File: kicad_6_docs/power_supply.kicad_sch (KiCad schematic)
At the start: 56 parts, among them J7 iec_power_entry, T1 power_transformer, U1 RC4558, U10 RC4558, U11 TL072, U12 TL072, U13 TL072, U14 SSI2164, U15 TL072, U16 TL072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

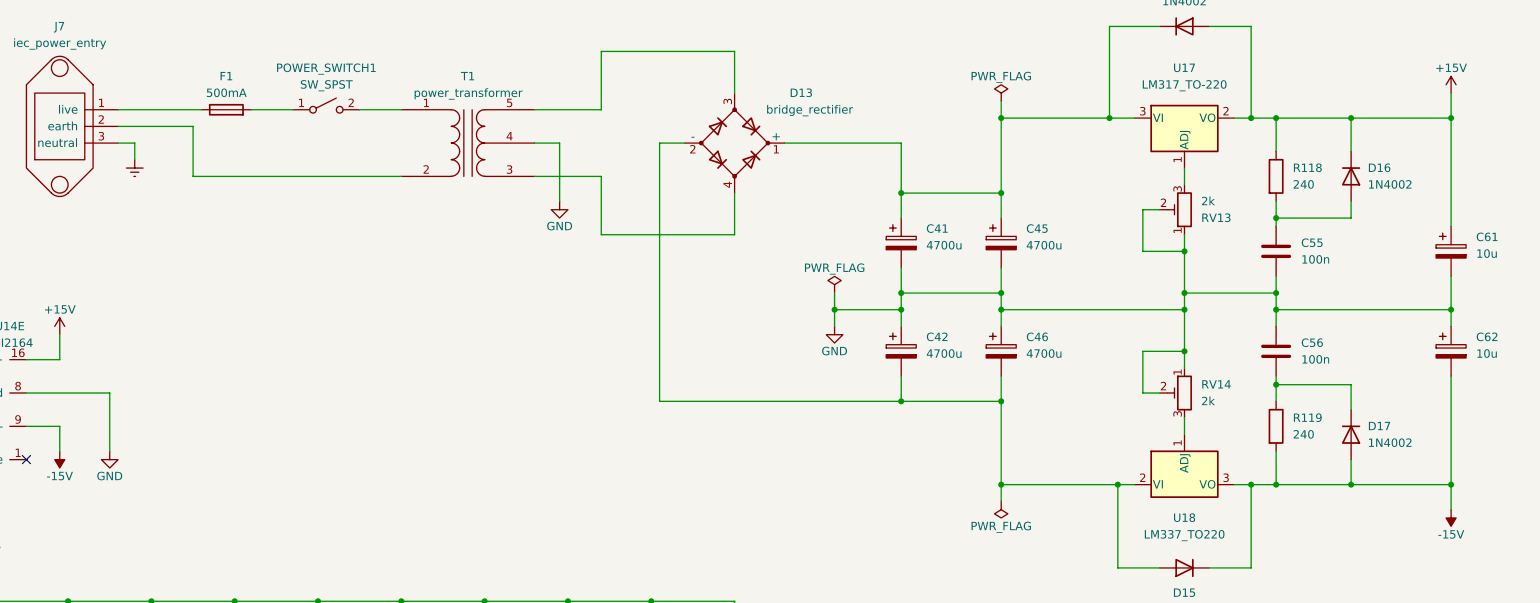
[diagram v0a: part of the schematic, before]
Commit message: Fix power supply errors, tidy up schematic
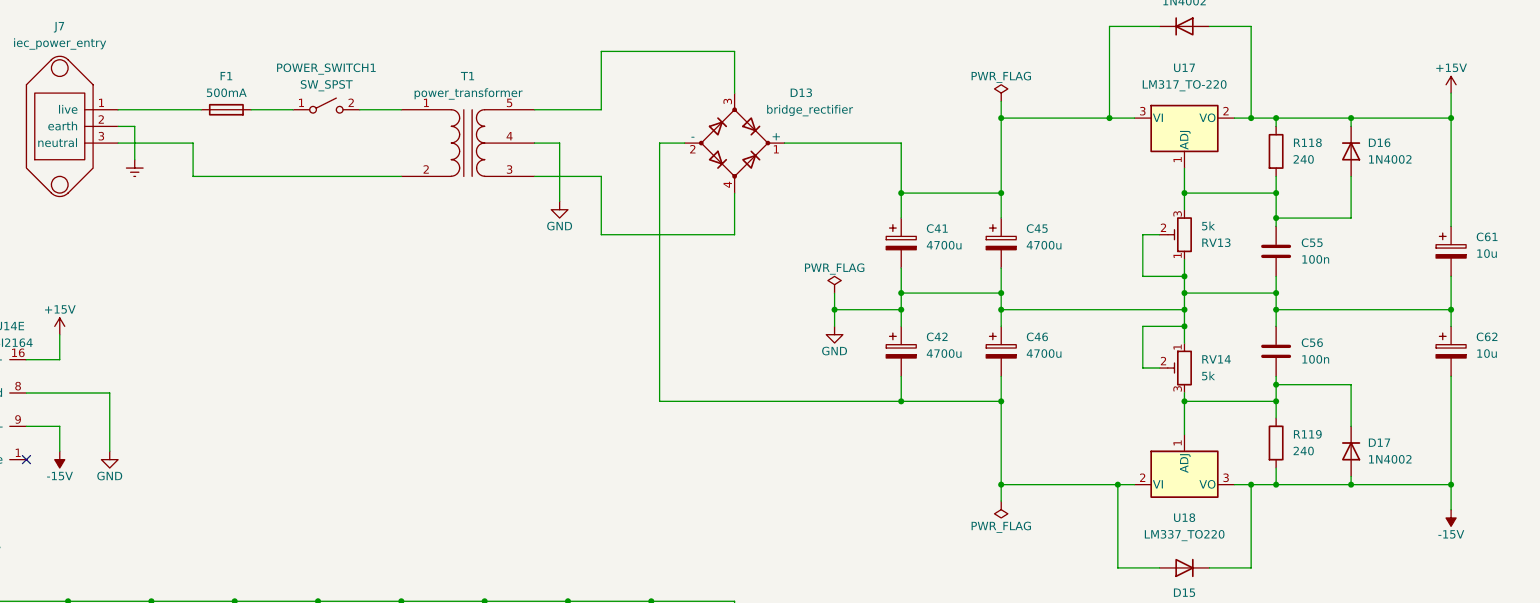
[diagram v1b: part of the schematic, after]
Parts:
- RV13, RV14: value 2k -> 5k
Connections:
- net Earth: now also J7.2 (earth); no longer J7.3 (neutral)
- net at RV14.3, U18.1 (ADJ): now also C56.2, D17.1 (K), R119.1
- net at T1.2 (AB): now also J7.3 (neutral); no longer J7.2 (earth)
- net at C55.1, D16.2 (A), R118.2: now also RV13.3, U17.1 (ADJ)
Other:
- moved on the sheet: D16, D17, R118, R119, RV13, RV14
